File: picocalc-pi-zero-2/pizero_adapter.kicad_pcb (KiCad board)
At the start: 2 copper layers, 29 x 51.8 mm, 3 parts, among them J1 Conn_01x20, J2 Conn_01x20, J3 Conn_02x20_Odd_Even

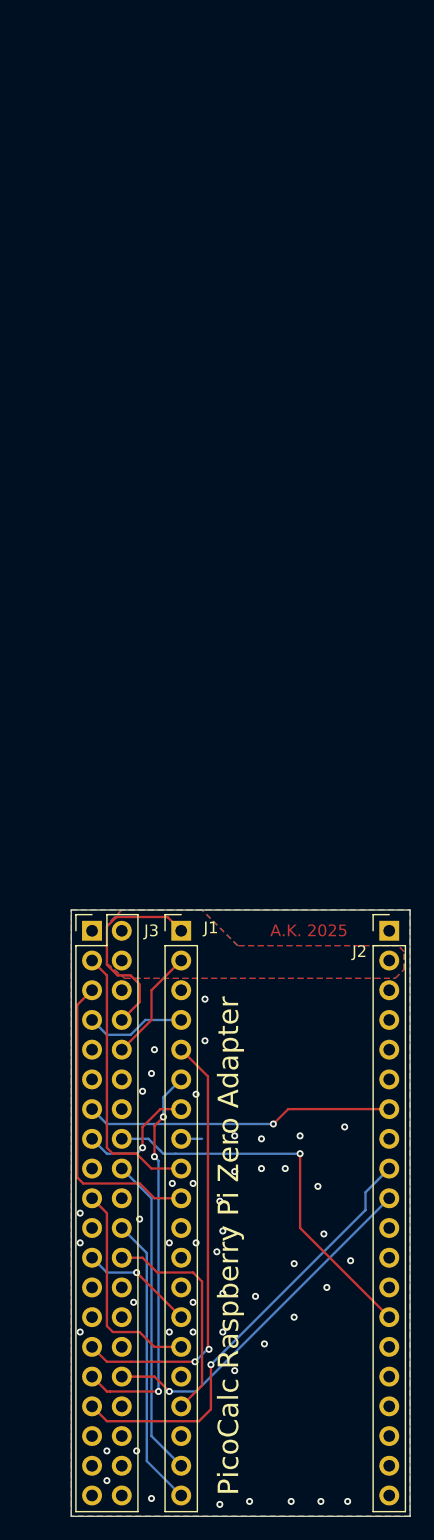
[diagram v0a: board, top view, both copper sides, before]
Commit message: picocalc-pi-zero-2: move rpi to clear the case
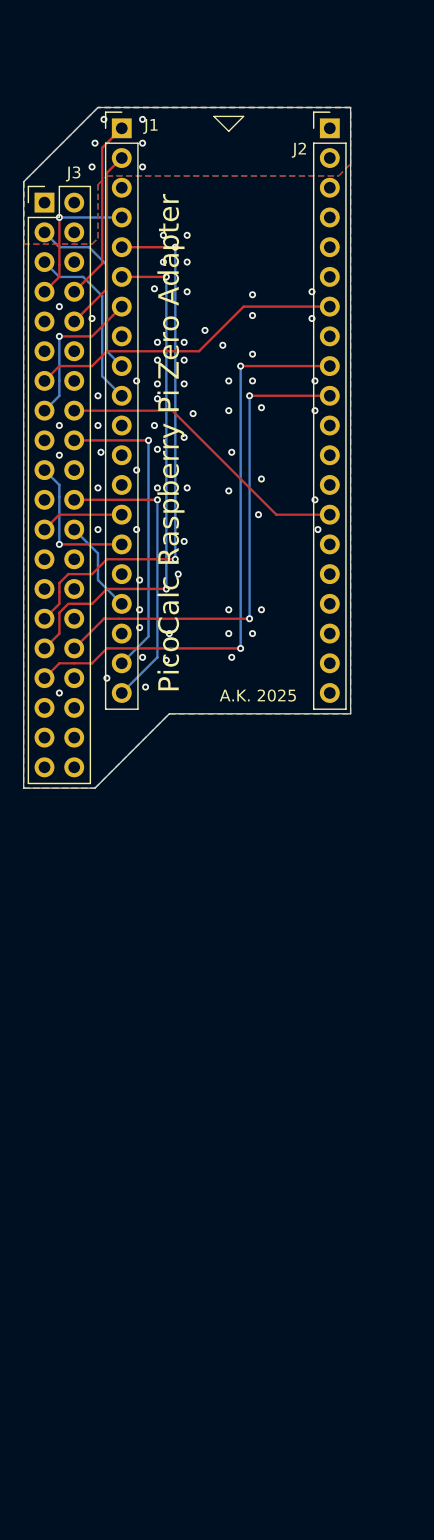
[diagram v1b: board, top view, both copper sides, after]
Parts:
- moved J1 68.8 mm to (96.5, 33.0)
- moved J2 68.8 mm to (114.3, 33.0)
- moved J3 62.4 mm to (89.9, 39.4)
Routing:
- net /PWM_L: track 30.2 -> 41.9 mm, vias 1 -> 2
- net /PWM_R: track 38.0 -> 49.6 mm, vias 1 -> 2
- net /~{SPI1_CS}: track 19.1 -> 8.03 mm
- net /I2C1_SCL: track 26.2 -> 15.4 mm
- net /GP4: track 34.0 -> 44.0 mm, vias 3 -> 2
- net /GP3: track 37.6 -> 45.6 mm
- net /I2C1_SDA: track 23.6 -> 15.7 mm
- net /GP21: track 32.9 -> 25.5 mm, vias 1 -> 0
- net /SPI1_TX: track 18.5 -> 12.2 mm, vias 0 -> 1
- net /UART0_RX: track 9.72 -> 15.7 mm
- net /GP2: track 8.67 -> 12.2 mm, vias 0 -> 1
- net /SPI1_SCK: track 9.72 -> 7.13 mm, vias 1 -> 0
- net /GP5: track 10.8 -> 13.3 mm
- net /UART0_TX: track 17.6 -> 15.7 mm
- net GND: track 1.78 -> 0.00 mm, vias 48 -> 66
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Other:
- board size 29 x 51.8 mm -> 27.9 x 58.2 mm
